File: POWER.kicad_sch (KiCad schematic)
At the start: 54 parts

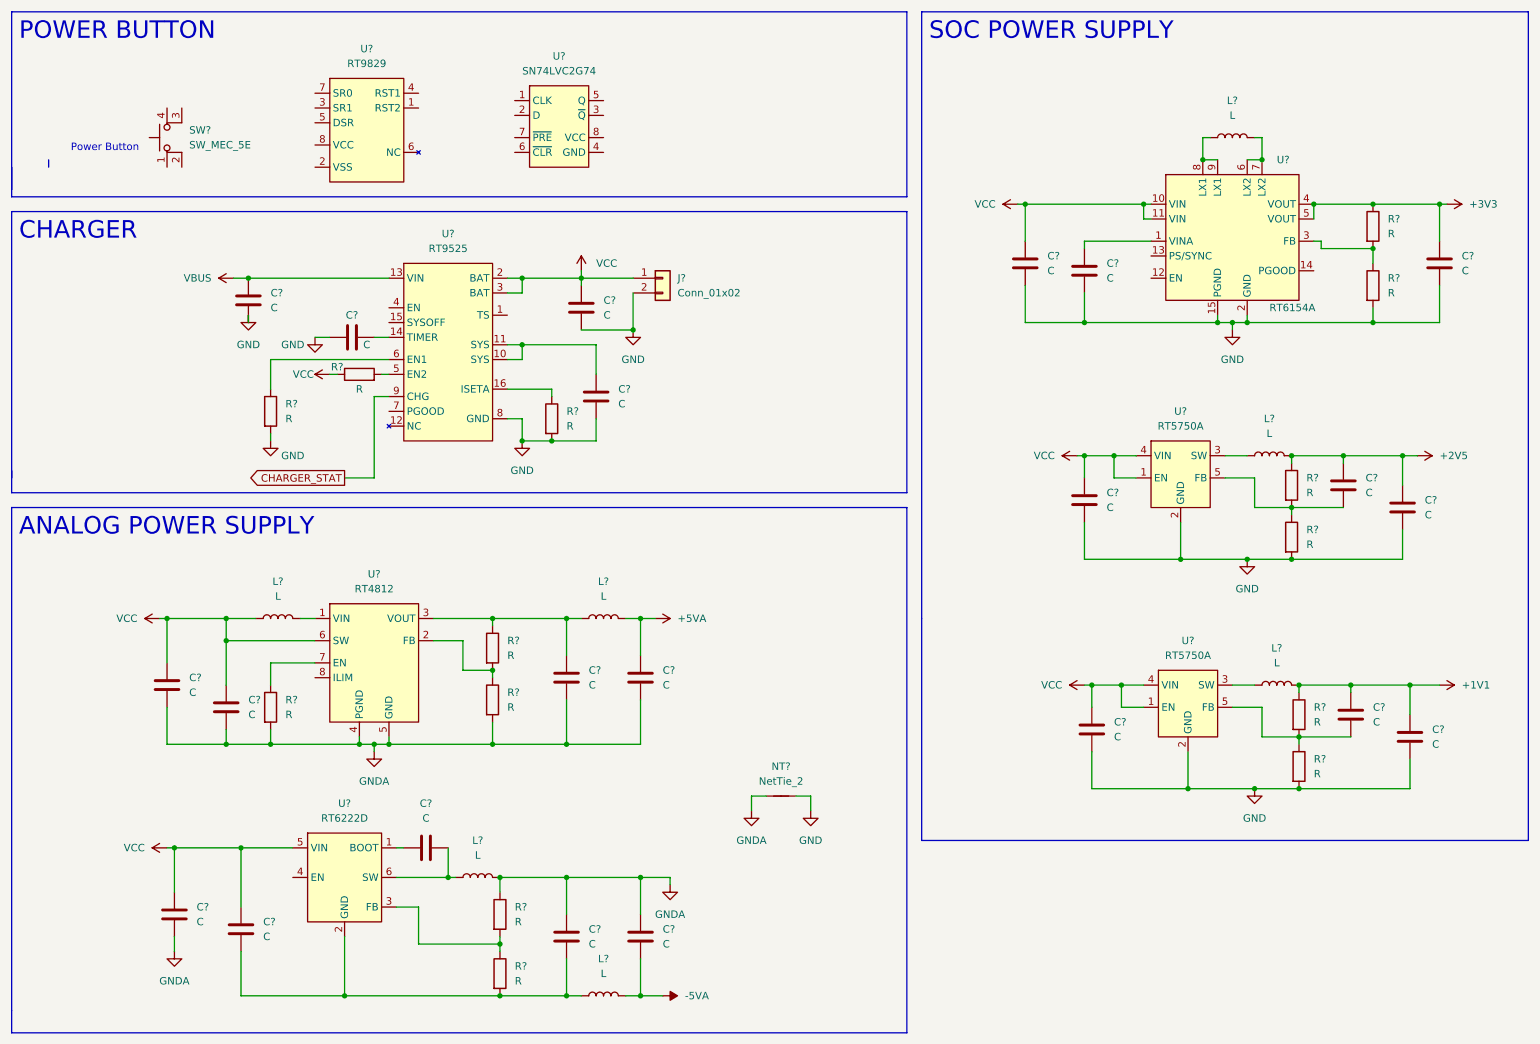
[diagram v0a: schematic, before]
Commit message: added SOC list
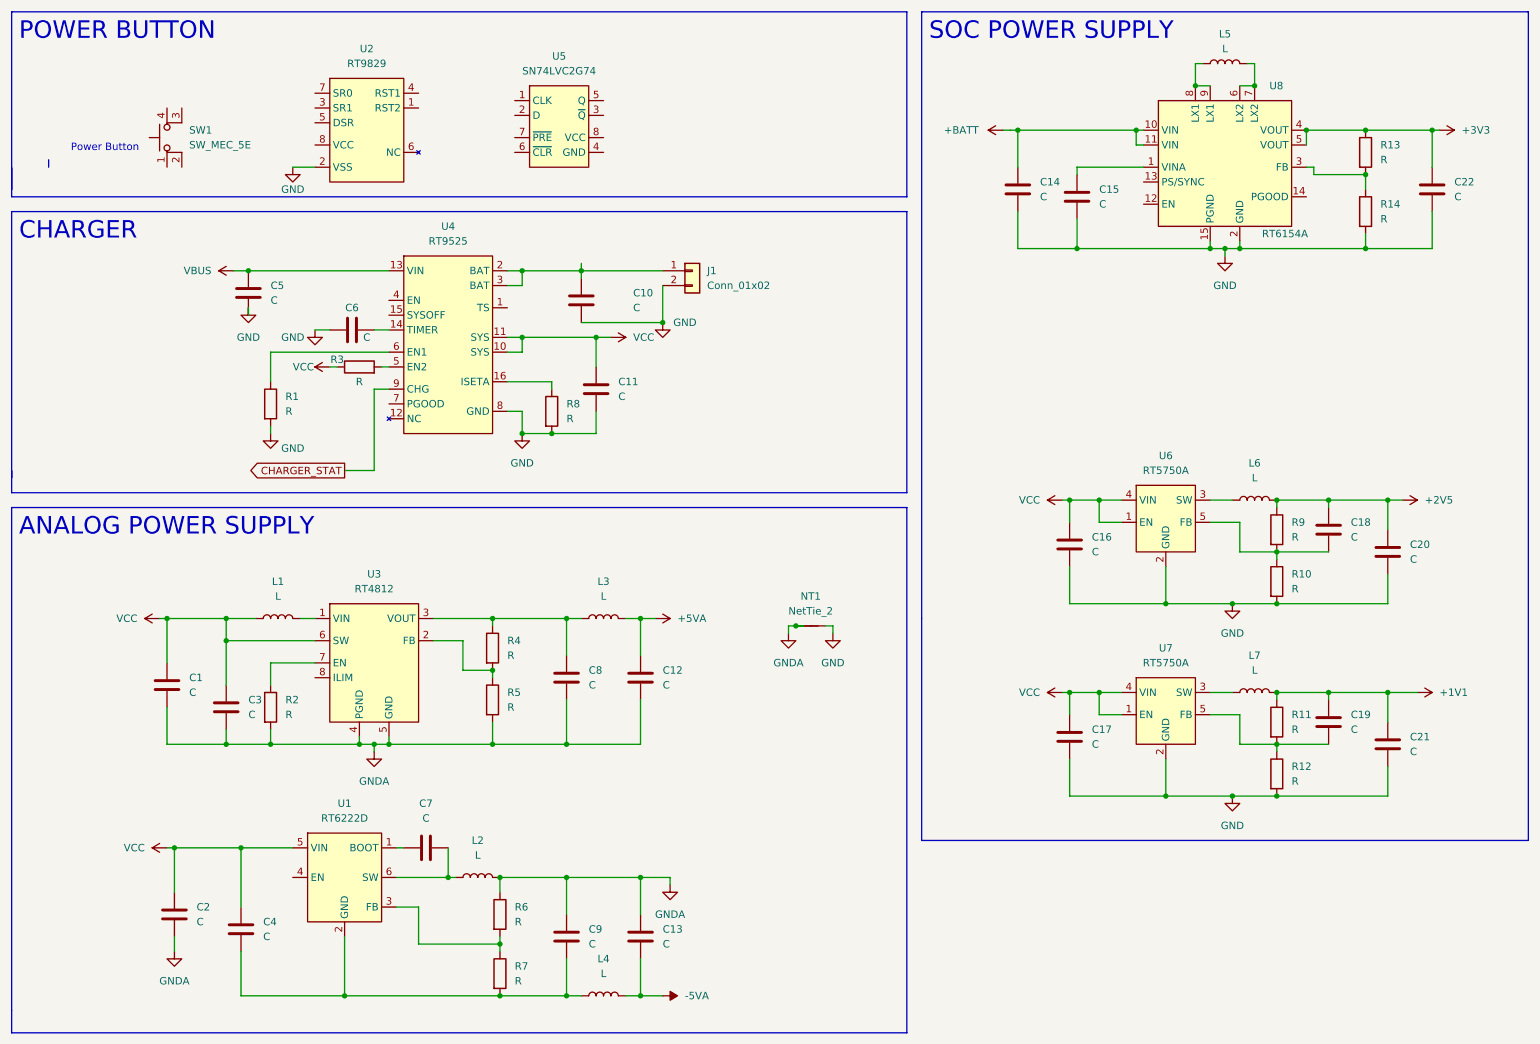
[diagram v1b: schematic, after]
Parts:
- C1, C10, C11, C12, C13, C14, C15, C16, C17, C18, C19, C2, C20, C21, C22, C3, C4, C5, C6, C7, C8, C9: renamed from C?; symbol Device:C -> rlib_passive:C
- L1, L2, L3, L4, L5, L6, L7: renamed from L?; symbol Device:L -> rlib_passive:L
- R1, R10, R11, R12, R13, R14, R2, R3, R4, R5, R6, R7, R8, R9: renamed from R?; symbol Device:R -> rlib_passive:R
- gave numbers to parts that had none: 11
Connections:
- net GND: now also U2.2 (VSS)
- net VCC: now also C11.1, U4.10 (SYS), U4.11 (SYS); no longer C10.1, C14.1, J1.1 (Pin_1), U4.2 (BAT), U4.3 (BAT), U8.10 (VIN), U8.11 (VIN)
- new net: C10.1, J1.1 (Pin_1), U4.2 (BAT), U4.3 (BAT)
- new net +BATT: C14.1, U8.10 (VIN), U8.11 (VIN)
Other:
- moved on the sheet: C10, C11, C14, C15, C16, C17, C18, C19, C20, C21, C22, C5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

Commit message: dfdfasfasf
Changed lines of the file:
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@@
     (stroke (width 0) (type default) (color 0 0 0 1))
-  )
-  (wire (pts (xy 154.94 125.73) (xy 153.67 125.73))
-    (stroke (width 0) (type default) (color 0 0 0 0))
   )
   (wire (pts (xy 114.3 189.23) (xy 116.84 189.23))
     (stroke (width 0) (type default) (color 0 0 0 1))
   )
-  (wire (pts (xy 153.67 125.73) (xy 154.94 125.73))
+  (wire (pts (xy 154.94 125.73) (xy 156.21 125.73))
     (stroke (width 0) (type default) (color 0 0 0 1))
   )
@@
     (stroke (width 0) (type default) (color 0 0 0 0))
   )
-  (wire (pts (xy 152.4 127) (xy 152.4 125.73))
-    (stroke (width 0) (type default) (color 0 0 0 1))
-  )
   (wire (pts (xy 106.68 92.71) (xy 111.76 92.71))
     (stroke (width 0) (type default) (color 0 0 0 1))
@@
     (stroke (width 0) (type default) (color 0 0 0 1))
   )
-  (wire (pts (xy 160.02 127) (xy 160.02 125.73))
-    (stroke (width 0) (type default) (color 0 0 0 1))
-  )
   (wire (pts (xy 152.4 125.73) (xy 153.67 125.73))
     (stroke (width 0) (type default) (color 0 0 0 1))
@@
   (wire (pts (xy 255.27 109.22) (xy 255.27 104.14))
     (stroke (width 0) (type default) (color 0 0 0 1))
+  )
+  (wire (pts (xy 153.67 125.73) (xy 156.21 125.73))
+    (stroke (width 0) (type default) (color 0 0 0 0))
   )
   (wire (pts (xy 262.89 46.99) (xy 262.89 40.64))
@@
     (pin "1")
   )
-  (symbol (lib_id "power:GNDA") (at 152.4 127 0) (unit 1)
-    (in_bom yes) (on_board yes) (fields_autoplaced)
-    (property "Reference" "#PWR0102" (id 0) (at 152.4 133.35 0)
-      (effects (font (size 1.27 1.27)) hide)
-    )
-    (property "Value" "GNDA" (id 1) (at 152.4 132.08 0))
-    (property "Footprint" "" (id 2) (at 152.4 127 0)
-      (effects (font (size 1.27 1.27)) hide)
-    )
-    (property "Datasheet" "" (id 3) (at 152.4 127 0)
+  (symbol (lib_id "power:GNDA") (at 152.4 125.73 0) (unit 1)
+    (in_bom yes) (on_board yes) (fields_autoplaced)
+    (property "Reference" "#PWR0102" (id 0) (at 152.4 132.08 0)
+      (effects (font (size 1.27 1.27)) hide)
+    )
+    (property "Value" "GNDA" (id 1) (at 152.4 130.81 0))
+    (property "Footprint" "" (id 2) (at 152.4 125.73 0)
+      (effects (font (size 1.27 1.27)) hide)
+    )
+    (property "Datasheet" "" (id 3) (at 152.4 125.73 0)
       (effects (font (size 1.27 1.27)) hide)
     )
@@
   )
   (symbol (lib_id "rlib_passive:L") (at 232.41 104.14 90) (unit 1)
-    (in_bom yes) (on_board yes) (fields_autoplaced)
-    (property "Reference" "L6" (id 0) (at 232.41 97.79 90))
-    (property "Value" "L" (id 1) (at 232.41 100.33 90))
+    (in_bom yes) (on_board yes)
+    (property "Reference" "L6" (id 0) (at 232.41 101.6 90))
+    (property "Value" "L" (id 1) (at 232.41 105.41 90))
     (property "Footprint" "" (id 2) (at 232.41 104.14 0)
       (effects (font (size 1.27 1.27)) hide)
@@
     (pin "2")
   )
-  (symbol (lib_id "power:GND") (at 160.02 127 0) (unit 1)
-    (in_bom yes) (on_board yes) (fields_autoplaced)
-    (property "Reference" "#PWR0103" (id 0) (at 160.02 133.35 0)
-      (effects (font (size 1.27 1.27)) hide)
-    )
-    (property "Value" "GND" (id 1) (at 160.02 132.08 0))
-    (property "Footprint" "" (id 2) (at 160.02 127 0)
-      (effects (font (size 1.27 1.27)) hide)
-    )
-    (property "Datasheet" "" (id 3) (at 160.02 127 0)
+  (symbol (lib_id "power:GND") (at 160.02 125.73 0) (unit 1)
+    (in_bom yes) (on_board yes) (fields_autoplaced)
+    (property "Reference" "#PWR0103" (id 0) (at 160.02 132.08 0)
+      (effects (font (size 1.27 1.27)) hide)
+    )
+    (property "Value" "GND" (id 1) (at 160.02 130.81 0))
+    (property "Footprint" "" (id 2) (at 160.02 125.73 0)
+      (effects (font (size 1.27 1.27)) hide)
+    )
+    (property "Datasheet" "" (id 3) (at 160.02 125.73 0)
       (effects (font (size 1.27 1.27)) hide)
     )
@@
   )
   (symbol (lib_id "rlib_passive:L") (at 232.41 137.16 90) (unit 1)
-    (in_bom yes) (on_board yes) (fields_autoplaced)
-    (property "Reference" "L7" (id 0) (at 232.41 130.81 90))
-    (property "Value" "L" (id 1) (at 232.41 133.35 90))
+    (in_bom yes) (on_board yes)
+    (property "Reference" "L7" (id 0) (at 232.41 134.62 90))
+    (property "Value" "L" (id 1) (at 232.41 138.43 90))
     (property "Footprint" "" (id 2) (at 232.41 137.16 0)
       (effects (font (size 1.27 1.27)) hide)

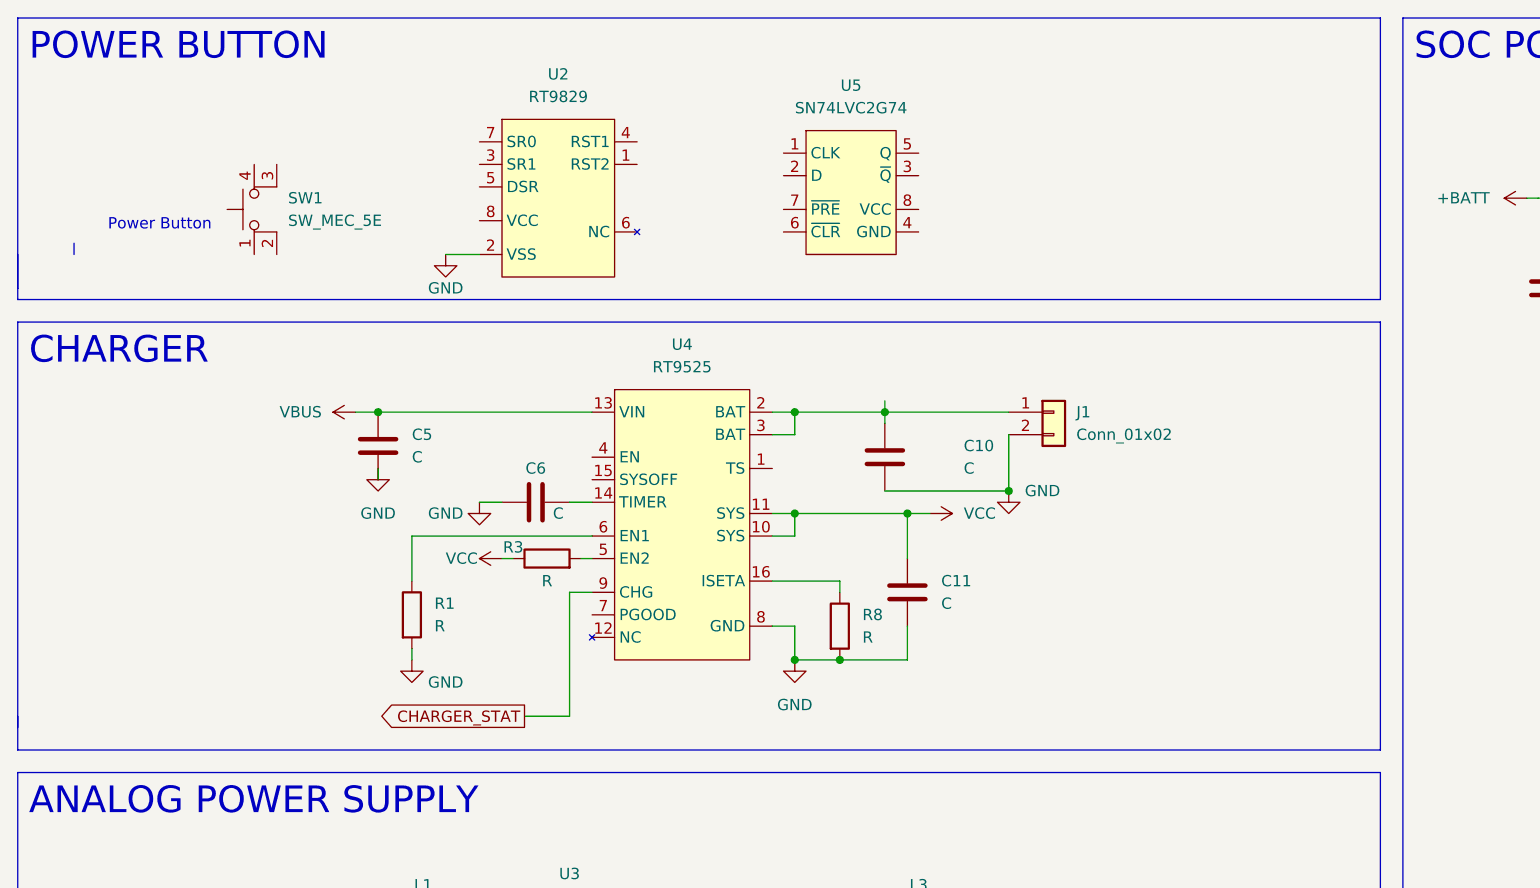
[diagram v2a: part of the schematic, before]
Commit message: replaced charger
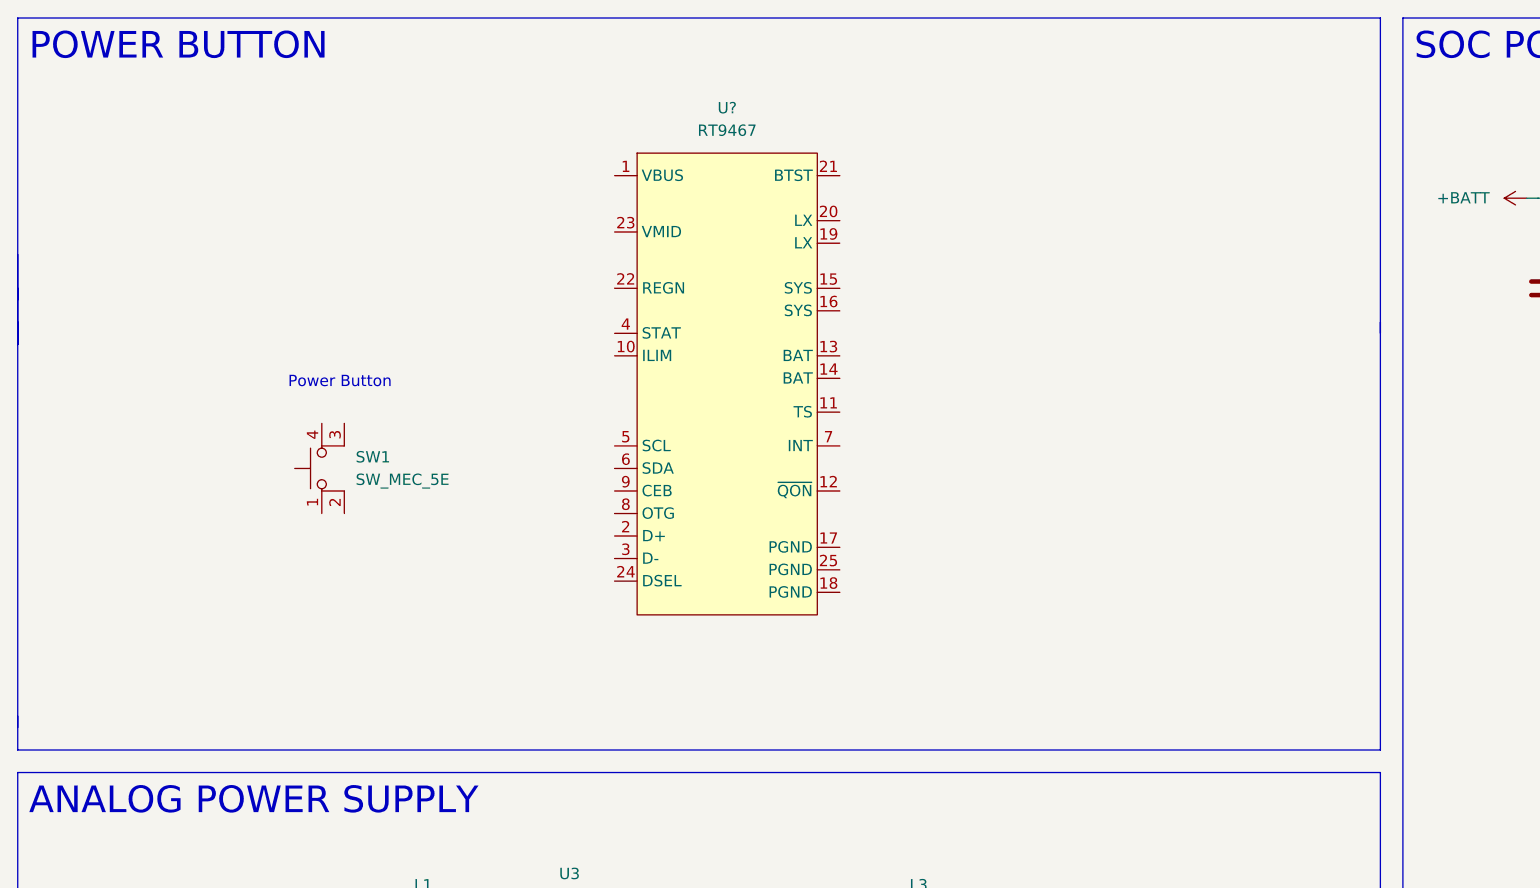
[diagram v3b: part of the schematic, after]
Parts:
- removed C10, C11, C5, C6: C, symbol rlib_passive:C
- removed J1: Conn_01x02, symbol Connector_Generic:Conn_01x02
- removed R1, R3, R8: R, symbol rlib_passive:R
- removed U2: RT9829, Package_DFN_QFN:DFN-8_2x2mm_P0.5mm, symbol rlib_power:RT9829
- removed U4: RT9525, Package_DFN_QFN:QFN-16-1EP_3x3mm_P0.5mm_EP1.45x1.45mm, symbol rlib_power:RT9525
- removed U5: SN74LVC2G74, Package_SO:SSOP-8_3.9x5.05mm_P1.27mm, symbol rlib_ic:SN74LVC2G74
- added U?: RT9467, Package_DFN_QFN:WQFN-24-1EP_4x4mm_P0.5mm_EP2.45x2.45mm, symbol rlib_power:RT9467
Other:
- note removed: "CHARGER"
- moved on the sheet: SW1
